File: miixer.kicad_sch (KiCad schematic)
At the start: 0 parts

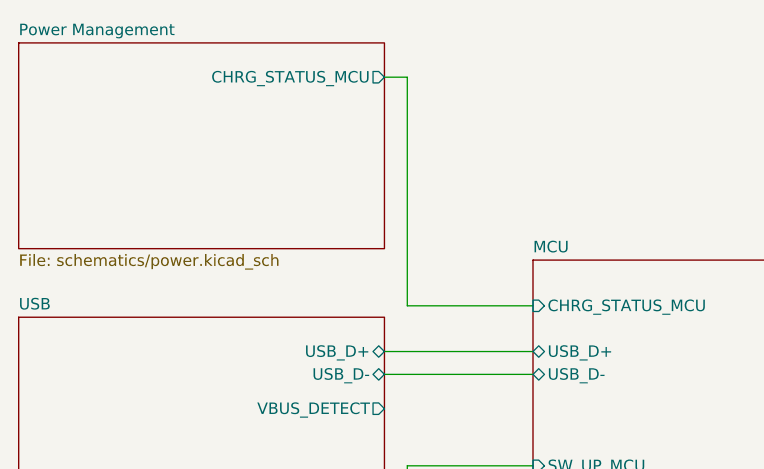
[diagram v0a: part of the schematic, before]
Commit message: Update colors
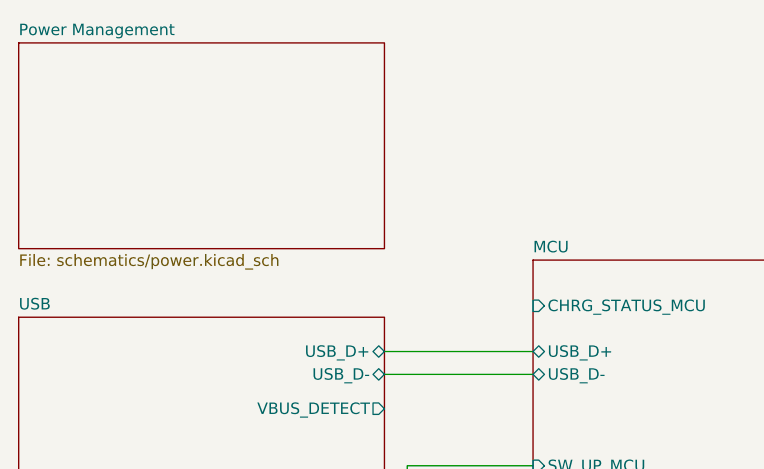
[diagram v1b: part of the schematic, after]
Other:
- sheet Power Management ports: added none; removed CHRG_STATUS_MCU
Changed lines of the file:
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@@
-	(wire
-		(pts
-			(xy 119.38 62.23) (xy 121.92 62.23)
-		)
-		(stroke
-			(width 0)
-			(type default)
-		)
-	)
 	(wire
 		(pts
@@
 	(wire
 		(pts
-			(xy 121.92 87.63) (xy 135.89 87.63)
-		)
-		(stroke
-			(width 0)
-			(type default)
-		)
-	)
-	(wire
-		(pts
 			(xy 119.38 133.35) (xy 129.54 133.35)
 		)
@@
 		(pts
 			(xy 124.46 128.27) (xy 124.46 107.95)
-		)
-		(stroke
-			(width 0)
-			(type default)
-		)
-	)
-	(wire
-		(pts
-			(xy 121.92 62.23) (xy 121.92 87.63)
 		)
 		(stroke
@@
 			)
 		)
-		(pin "CHRG_STATUS_MCU" output
-			(at 119.38 62.23 0)
-			(effects
-				(font
-					(size 1.27 1.27)
-				)
-				(justify right)
-			)
-		)

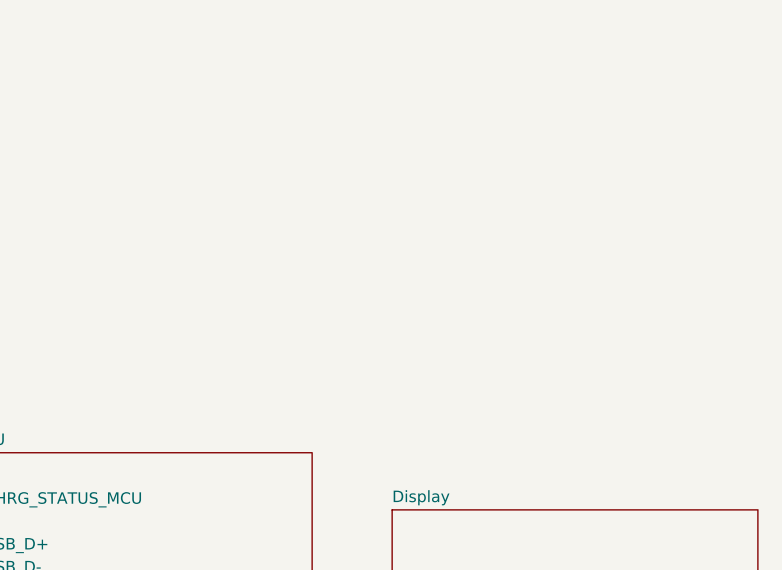
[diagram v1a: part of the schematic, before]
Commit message: Update power traces
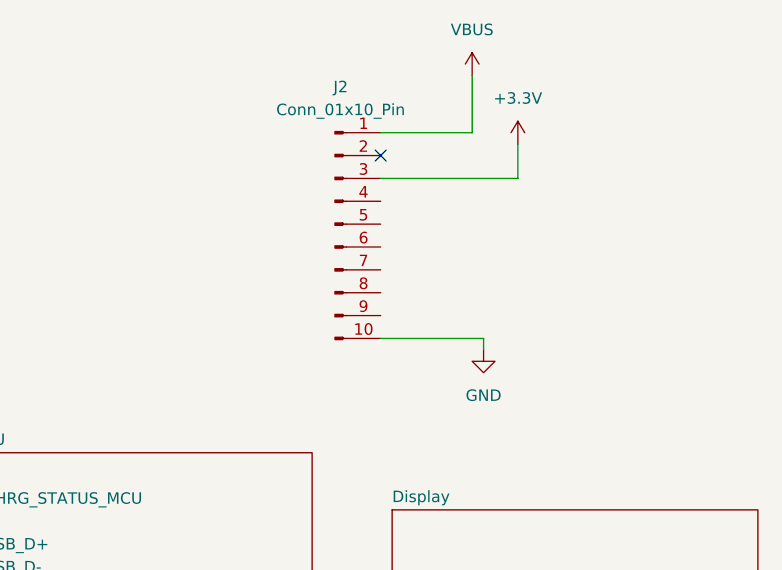
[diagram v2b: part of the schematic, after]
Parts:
- added J2: Conn_01x10_Pin, Connector_PinHeader_2.54mm:PinHeader_1x10_P2.54mm_Vertical, symbol Connector:Conn_01x10_Pin
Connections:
- new net +3.3V: J2.3 (Pin_3)
- new net GND: J2.10 (Pin_10)
- new net VBUS: J2.1 (Pin_1)
- no-connect marks 0 -> 1

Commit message: Update README
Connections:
- net SDA: now reaches J2.4 (Pin_4)
- net SCL: now reaches J2.5 (Pin_5)
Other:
- removed sheet Display
- sheet Buttons ports: added LED_MCU, SCL, SDA; removed SW_CENTER_MCU, SW_DOWN_MCU, SW_LEFT_MCU, SW_RIGHT_MCU, SW_UP_MCU
- sheet MCU ports: added LED_MCU, SCL_MCU, SDA_MCU; removed CHRG_STATUS_MCU, SW_CENTER_MCU, SW_DOWN_MCU, SW_LEFT_MCU, SW_RIGHT_MCU, SW_UP_MCU
- sheet USB ports: added none; removed VBUS_DETECT
- moved on the sheet: J2
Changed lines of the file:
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@@
 	(paper "A4")
 	(no_connect
-		(at 181.61 49.53)
-	)
-	(wire
-		(pts
-			(xy 196.85 52.07) (xy 196.85 48.26)
+		(at 195.58 93.98)
+	)
+	(wire
+		(pts
+			(xy 210.82 96.52) (xy 210.82 92.71)
 		)
 		(stroke
@@
 	(wire
 		(pts
-			(xy 193.04 69.85) (xy 193.04 71.12)
+			(xy 207.01 114.3) (xy 207.01 115.57)
 		)
 		(stroke
@@
 	(wire
 		(pts
+			(xy 121.92 105.41) (xy 135.89 105.41)
+		)
+		(stroke
+			(width 0)
+			(type default)
+		)
+	)
+	(wire
+		(pts
 			(xy 135.89 115.57) (xy 132.08 115.57)
 		)
@@
 	(wire
 		(pts
+			(xy 124.46 107.95) (xy 135.89 107.95)
+		)
+		(stroke
+			(width 0)
+			(type default)
+		)
+	)
+	(wire
+		(pts
 			(xy 119.38 135.89) (xy 132.08 135.89)
 		)
@@
 	(wire
 		(pts
-			(xy 121.92 105.41) (xy 135.89 105.41)
-		)
-		(stroke
-			(width 0)
-			(type default)
-		)
-	)
-	(wire
-		(pts
-			(xy 181.61 46.99) (xy 191.77 46.99)
+			(xy 195.58 91.44) (xy 205.74 91.44)
+		)
+		(stroke
+			(width 0)
+			(type default)
+		)
+	)
+	(wire
+		(pts
+			(xy 195.58 99.06) (xy 200.66 99.06)
 		)
 		(stroke
@@
 	(wire
 		(pts
-			(xy 191.77 46.99) (xy 191.77 40.64)
+			(xy 205.74 91.44) (xy 205.74 85.09)
 		)
 		(stroke
@@
 	(wire
 		(pts
-			(xy 181.61 69.85) (xy 193.04 69.85)
+			(xy 195.58 114.3) (xy 207.01 114.3)
+		)
+		(stroke
+			(width 0)
+			(type default)
+		)
+	)
+	(wire
+		(pts
+			(xy 195.58 101.6) (xy 200.66 101.6)
 		)
 		(stroke
@@
 	(wire
 		(pts
-			(xy 124.46 107.95) (xy 135.89 107.95)
-		)
-		(stroke
-			(width 0)
-			(type default)
-		)
-	)
-	(wire
-		(pts
-			(xy 181.61 52.07) (xy 196.85 52.07)
+			(xy 195.58 96.52) (xy 210.82 96.52)
 		)
 		(stroke
@@
 			(width 0)
 			(type default)
+		)
+	)
+	(label "SCL"
+		(at 200.66 101.6 0)
+		(effects
+			(font
+				(size 1.27 1.27)
+			)
+			(justify left bottom)
+		)
+	)
+	(label "SDA"
+		(at 200.66 99.06 0)
+		(effects
+			(font
+				(size 1.27 1.27)
+			)
+			(justify left bottom)
+		)
+	)
+	(label "SCL"
+		(at 127 107.95 0)
+		(effects
+			(font
+				(size 1.27 1.27)
+			)
+			(justify left bottom)
+		)
+	)
+	(label "SDA"
+		(at 127 105.41 0)
+		(effects
+			(font
+				(size 1.27 1.27)
+			)
+			(justify left bottom)
 		)
 	)
 	(symbol
 		(lib_id "Connector:Conn_01x10_Pin")
-		(at 176.53 57.15 0)
+		(at 190.5 101.6 0)
 		(unit 1)
 		(exclude_from_sim no)
@@
 		(fields_autoplaced yes)
 		(property "Reference" "J2"
-			(at 177.165 41.91 0)
+			(at 191.135 86.36 0)
 			(effects
 				(font
@@
 		)
 		(property "Value" "Conn_01x10_Pin"
-			(at 177.165 44.45 0)
+			(at 191.135 88.9 0)
 			(effects
 				(font
@@
 		)
 		(property "Footprint" "Connector_PinHeader_2.54mm:PinHeader_1x10_P2.54mm_Vertical"
-			(at 176.53 57.15 0)
+			(at 190.5 101.6 0)
 			(effects
 				(font
@@
 		)
 		(property "Datasheet" "~"
-			(at 176.53 57.15 0)
+			(at 190.5 101.6 0)
 			(effects
 				(font
@@
 		)
 		(property "Description" "Generic connector, single row, 01x10, script generated"
-			(at 176.53 57.15 0)
+			(at 190.5 101.6 0)
 			(effects
 				(font
@@
 	(symbol
 		(lib_id "power:+3.3V")
-		(at 196.85 48.26 0)
+		(at 210.82 92.71 0)
 		(unit 1)
 		(exclude_from_sim no)
@@
 		(fields_autoplaced yes)
 		(property "Reference" "#PWR031"
-			(at 196.85 52.07 0)
+			(at 210.82 96.52 0)
 			(effects
 				(font
@@
 		)
 		(property "Value" "+3.3V"
-			(at 196.85 43.18 0)
+			(at 210.82 87.63 0)
 			(effects
 				(font
@@
 		)
 		(property "Footprint" ""
-			(at 196.85 48.26 0)
+			(at 210.82 92.71 0)
 			(effects
 				(font
@@
 		)
 		(property "Datasheet" ""
-			(at 196.85 48.26 0)
+			(at 210.82 92.71 0)
 			(effects
 				(font
@@
 		)
 		(property "Description" "Power symbol creates a global label with name \"+3.3V\""
-			(at 196.85 48.26 0)
+			(at 210.82 92.71 0)
 			(effects
 				(font
@@
 	(symbol
 		(lib_id "power:GND")
-		(at 193.04 71.12 0)
+		(at 207.01 115.57 0)
 		(unit 1)
 		(exclude_from_sim no)
@@
 		(fields_autoplaced yes)
 		(property "Reference" "#PWR034"
-			(at 193.04 77.47 0)
+			(at 207.01 121.92 0)
 			(effects
 				(font
@@
 		)
 		(property "Value" "GND"
-			(at 193.04 76.2 0)
+			(at 207.01 120.65 0)
 			(effects
 				(font
@@
 		)
 		(property "Footprint" ""
-			(at 193.04 71.12 0)
+			(at 207.01 115.57 0)
 			(effects
 				(font
@@
 		)
 		(property "Datasheet" ""
-			(at 193.04 71.12 0)
+			(at 207.01 115.57 0)
 			(effects
 				(font
@@
 		)
 		(property "Description" "Power symbol creates a global label with name \"GND\" , ground"
-			(at 193.04 71.12 0)
+			(at 207.01 115.57 0)
 			(effects
 				(font
@@
 	(symbol
 		(lib_id "power:VBUS")
-		(at 191.77 40.64 0)
+		(at 205.74 85.09 0)
 		(unit 1)
 		(exclude_from_sim no)
@@
 		(fields_autoplaced yes)
 		(property "Reference" "#PWR033"
-			(at 191.77 44.45 0)
+			(at 205.74 88.9 0)
 			(effects
 				(font
@@
 		)
 		(property "Value" "VBUS"
-			(at 191.77 35.56 0)
+			(at 205.74 80.01 0)
 			(effects
 				(font
@@
 		)
 		(property "Footprint" ""
-			(at 191.77 40.64 0)
+			(at 205.74 85.09 0)
 			(effects
 				(font
@@
 		)
 		(property "Datasheet" ""
-			(at 191.77 40.64 0)
+			(at 205.74 85.09 0)
 			(effects
 				(font
@@
 		)
 		(property "Description" "Power symbol creates a global label with name \"VBUS\""
-			(at 191.77 40.64 0)
+			(at 205.74 85.09 0)
 			(effects
 				(font
@@
 					(reference "#PWR033")
 					(unit 1)
-				)
-			)
-		)
-	)
-	(sheet
-		(at 182.88 88.9)
-		(size 40.64 22.86)
-		(exclude_from_sim no)
-		(in_bom yes)
-		(on_board yes)
-		(dnp no)
-		(fields_autoplaced yes)
-		(stroke
-			(width 0.1524)
-			(type solid)
-		)
-		(fill
-			(color 0 0 0 0.0000)
-		)
-		(property "Sheetname" "Display"
-			(at 182.88 88.1884 0)
-			(effects
-				(font
-					(size 1.27 1.27)
-				)
-				(justify left bottom)
-			)
-		)
-		(property "Sheetfile" "schematics/display.kicad_sch"
-			(at 182.88 112.3446 0)
-			(effects
-				(font
-					(size 1.27 1.27)
-				)
-				(justify left top)
-			)
-		)
-		(instances
-			(project "miixer"
-				(path "/f2af4cd4-99cf-4d01-92f6-6413371e0fe3"
-					(page "3")
 				)
 			)
@@
 			)
 		)
-		(pin "SW_CENTER_MCU" input
-			(at 135.89 115.57 180)
+		(pin "SCL_MCU" bidirectional
+			(at 135.89 107.95 180)
 			(effects
 				(font
@@
 			)
 		)
-		(pin "SW_DOWN_MCU" input
-			(at 135.89 107.95 180)
+		(pin "SDA_MCU" bidirectional
+			(at 135.89 105.41 180)
 			(effects
 				(font
@@
 			)
 		)
-		(pin "SW_LEFT_MCU" input
+		(pin "LED_MCU" bidirectional
 			(at 135.89 110.49 180)
-			(effects
-				(font
-					(size 1.27 1.27)
-				)
-				(justify left)
-			)
-		)
-		(pin "SW_RIGHT_MCU" input
-			(at 135.89 113.03 180)
-			(effects
-				(font
-					(size 1.27 1.27)
-				)
-				(justify left)
-			)
-		)
-		(pin "SW_UP_MCU" input
-			(at 135.89 105.41 180)
-			(effects
-				(font
-					(size 1.27 1.27)
-				)
-				(justify left)
-			)
-		)
-		(pin "CHRG_STATUS_MCU" input
-			(at 135.89 87.63 180)
 			(effects
 				(font
@@
 			)
 		)
-		(pin "SW_CENTER_MCU" output
-			(at 119.38 135.89 0)
+		(pin "LED_MCU" bidirectional
+			(at 119.38 130.81 0)
 			(effects
 				(font
@@
 			)
 		)
-		(pin "SW_DOWN_MCU" output
+		(pin "SCL" bidirectional
 			(at 119.38 128.27 0)
 			(effects
@@
 			)
 		)
-		(pin "SW_LEFT_MCU" output
-			(at 119.38 130.81 0)
-			(effects
-				(font
-					(size 1.27 1.27)
-				)
-				(justify right)
-			)
-		)
-		(pin "SW_RIGHT_MCU" output
-			(at 119.38 133.35 0)
-			(effects
-				(font
-					(size 1.27 1.27)
-				)
-				(justify right)
-			)
-		)
-		(pin "SW_UP_MCU" output
+		(pin "SDA" bidirectional
 			(at 119.38 125.73 0)
 			(effects
@@
 			(effects
 				(font
-					(size 1.27 1.27)
-				)
-				(justify right)
-			)
-		)
-		(pin "VBUS_DETECT" output
-			(at 119.38 99.06 0)
-			(effects
-				(font

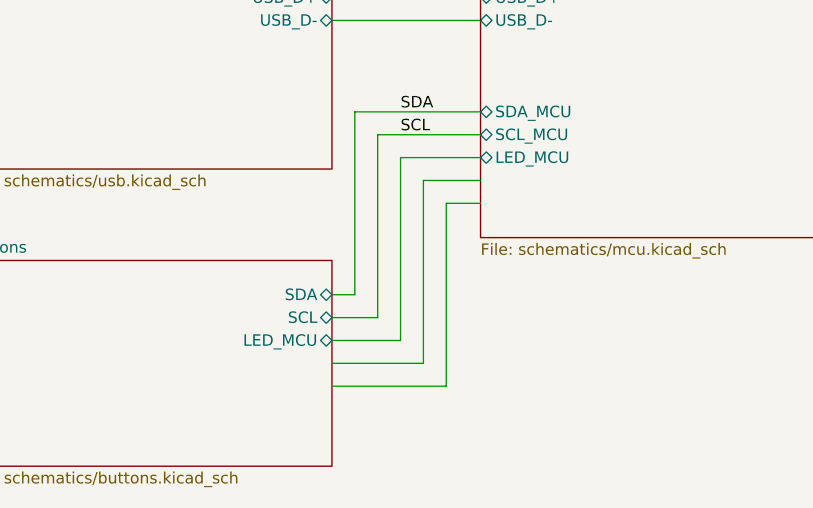
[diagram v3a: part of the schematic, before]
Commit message: Wire buttons
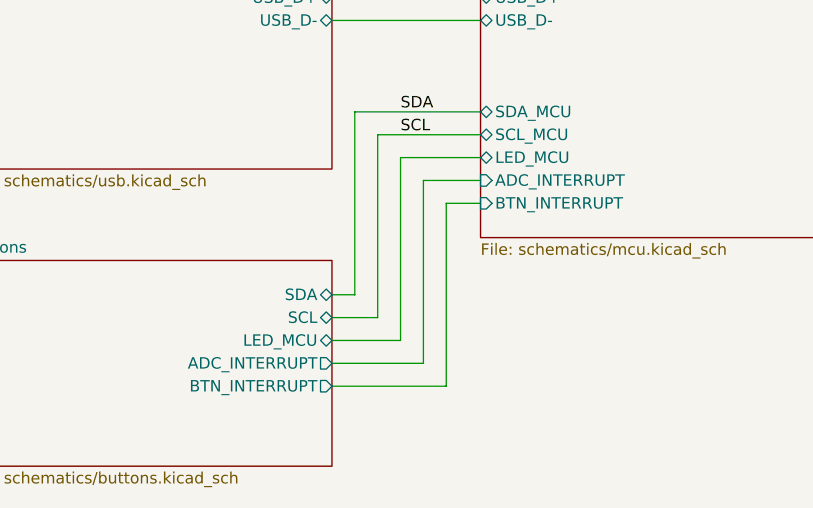
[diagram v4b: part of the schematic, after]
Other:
- sheet Buttons ports: added ADC_INTERRUPT, BTN_INTERRUPT; removed none
- sheet MCU ports: added ADC_INTERRUPT, BTN_INTERRUPT; removed none
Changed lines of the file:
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@@
+			)
+		)
+		(pin "ADC_INTERRUPT" input
+			(at 135.89 113.03 180)
+			(effects
+				(font
+					(size 1.27 1.27)
+				)
+				(justify left)
+			)
+		)
+		(pin "BTN_INTERRUPT" input
+			(at 135.89 115.57 180)
+			(effects
+				(font
+					(size 1.27 1.27)
+				)
+				(justify left)
 			)
 		)
@@
 			(effects
 				(font
+					(size 1.27 1.27)
+				)
+				(justify right)
+			)
+		)
+		(pin "ADC_INTERRUPT" output
+			(at 119.38 133.35 0)
+			(effects
+				(font
+					(size 1.27 1.27)
+				)
+				(justify right)
+			)
+		)
+		(pin "BTN_INTERRUPT" output
+			(at 119.38 135.89 0)
+			(effects
+				(font

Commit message: Update bom
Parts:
- J2: now not fitted
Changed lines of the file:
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@@
 		(in_bom yes)
 		(on_board yes)
-		(dnp no)
+		(dnp yes)
 		(fields_autoplaced yes)
 		(property "Reference" "J2"

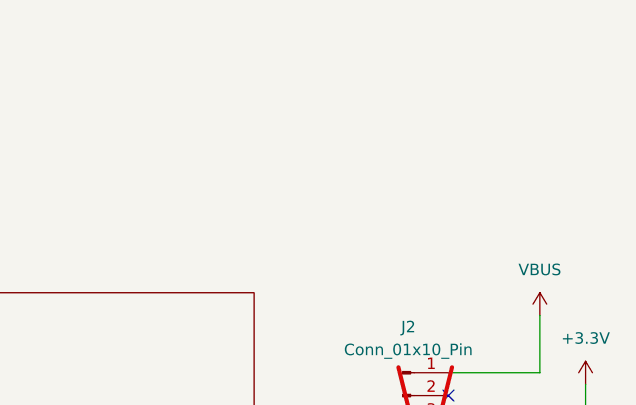
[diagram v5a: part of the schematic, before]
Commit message: Add QWIIC connector
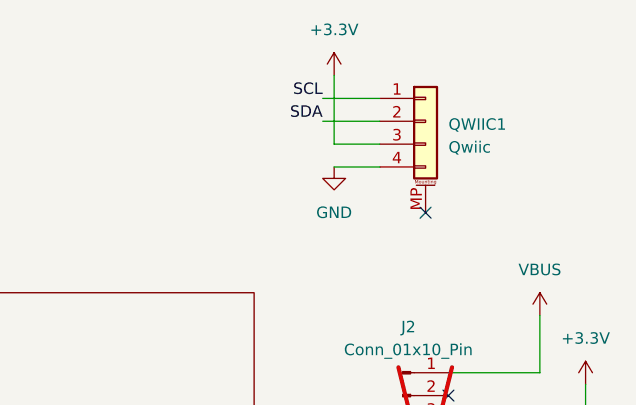
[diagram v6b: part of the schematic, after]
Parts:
- added QWIIC1: Qwiic, Connector_JST:JST_SH_SM04B-SRSS-TB_1x04-1MP_P1.00mm_Horizontal, symbol Connector_Generic_MountingPin:Conn_01x04_MountingPin
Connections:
- net +3.3V: now also QWIIC1.3 (Pin_3)
- net GND: now also QWIIC1.4 (Pin_4)
- net SCL: now also QWIIC1.1 (Pin_1)
- net SDA: now also QWIIC1.2 (Pin_2)
- no-connect marks 1 -> 2

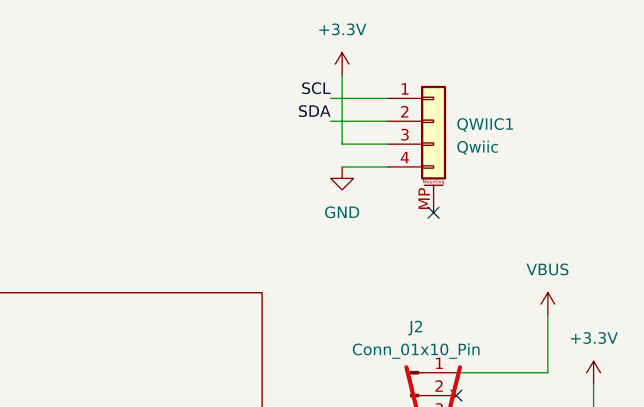
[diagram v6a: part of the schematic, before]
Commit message: Update QWIIC connector
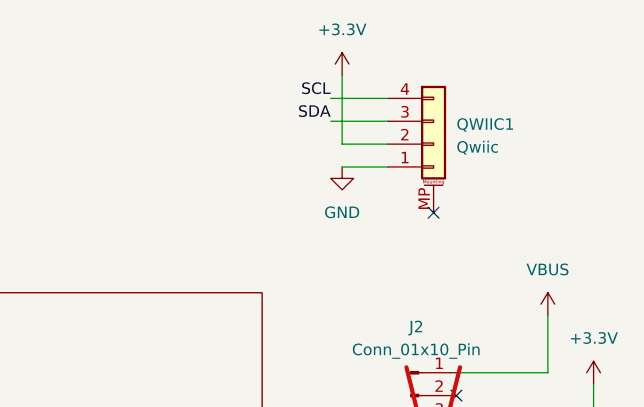
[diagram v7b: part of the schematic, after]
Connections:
- net +3.3V: now also QWIIC1.2 (Pin_2); no longer QWIIC1.3 (Pin_3)
- net GND: now also QWIIC1.1 (Pin_1); no longer QWIIC1.4 (Pin_4)
- net SCL: now also QWIIC1.4 (Pin_4); no longer QWIIC1.1 (Pin_1)
- net SDA: now also QWIIC1.3 (Pin_3); no longer QWIIC1.2 (Pin_2)
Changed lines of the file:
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@@
 		(property "Description" "Generic connectable mounting pin connector, single row, 01x04, script generated (kicad-library-utils/schlib/autogen/connector/)"
 			(at 193.04 63.5 0)
+			(show_name yes)
 			(effects
 				(font

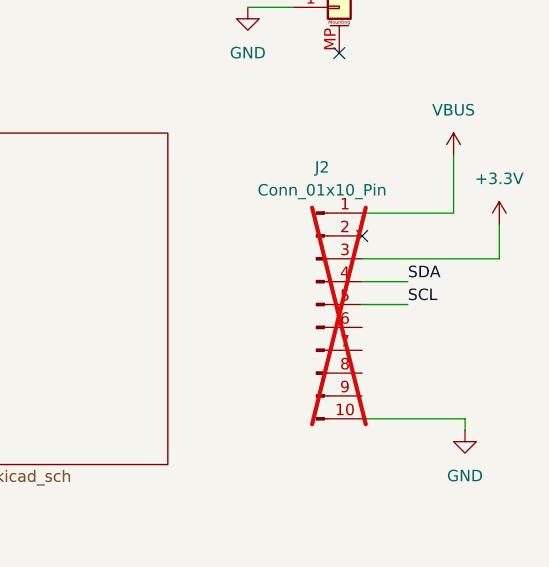
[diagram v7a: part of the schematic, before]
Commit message: Fix layout, rewiring, and clearances
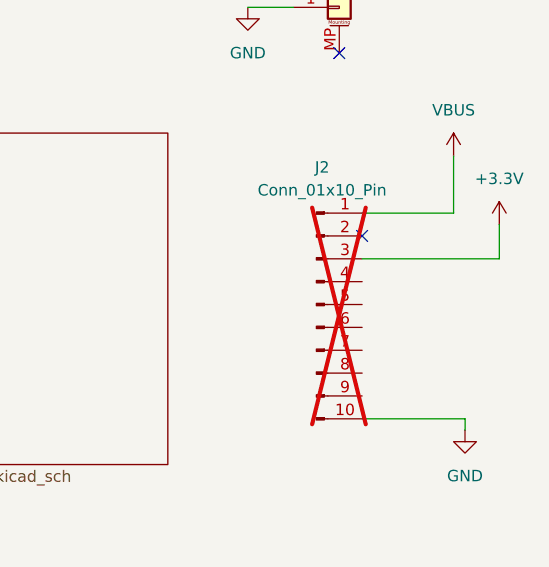
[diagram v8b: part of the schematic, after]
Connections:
- net SCL: no longer J2.5 (Pin_5)
- net SDA: no longer J2.4 (Pin_4)
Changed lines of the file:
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@@
-	(wire
-		(pts
-			(xy 195.58 99.06) (xy 200.66 99.06)
-		)
-		(stroke
-			(width 0)
-			(type default)
-		)
-	)
 	(wire
 		(pts
@@
 	(wire
 		(pts
-			(xy 195.58 101.6) (xy 200.66 101.6)
-		)
-		(stroke
-			(width 0)
-			(type default)
-		)
-	)
-	(wire
-		(pts
 			(xy 181.61 60.96) (xy 187.96 60.96)
 		)
@@
 		)
 	)
-	(label "SCL"
-		(at 200.66 101.6 0)
-		(effects
-			(font
-				(size 1.27 1.27)
-			)
-			(justify left bottom)
-		)
-	)
-	(label "SDA"
-		(at 200.66 99.06 0)
-		(effects
-			(font
-				(size 1.27 1.27)
-			)
-			(justify left bottom)
-		)
-	)
